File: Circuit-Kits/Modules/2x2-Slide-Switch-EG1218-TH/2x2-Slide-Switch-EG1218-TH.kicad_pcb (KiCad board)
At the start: 2 copper layers, 15.6 x 15.6 mm, 1 part, among them SW1 SPDT_Small

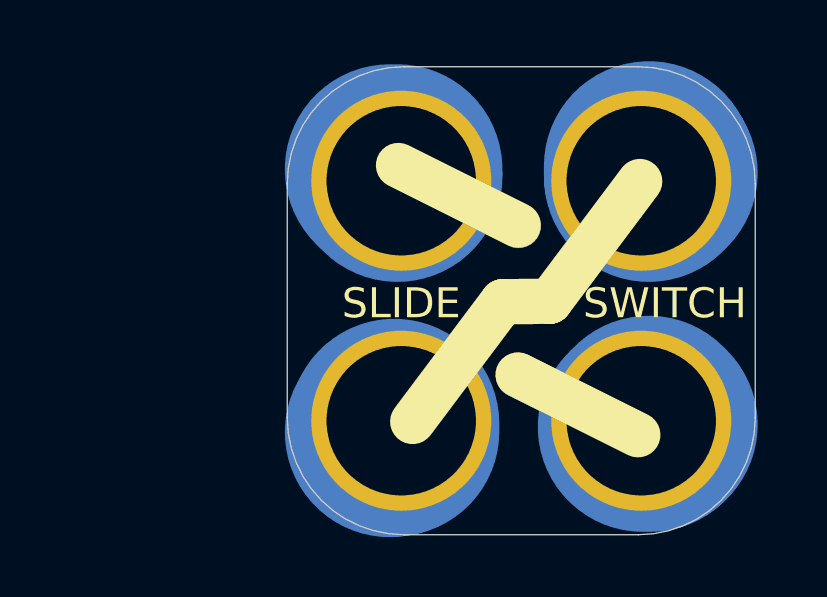
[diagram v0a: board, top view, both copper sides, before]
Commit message: Add top copper rings. Release v1.1 EG1218 TH 2x2
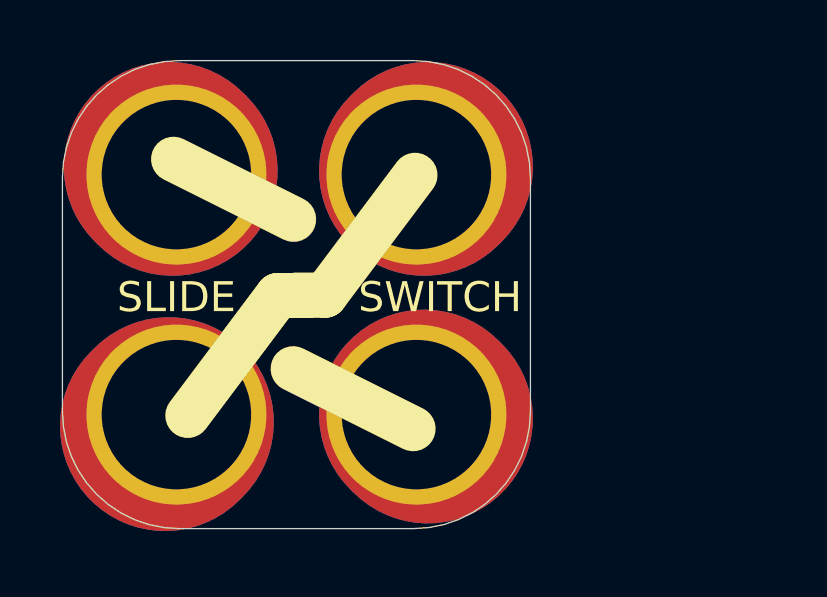
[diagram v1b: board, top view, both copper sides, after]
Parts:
- moved SW1 7.50 mm to (16.5, 57.9)
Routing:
- net /2: track 0.51 -> 0.00 mm
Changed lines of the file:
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@@
     (links 4)
     (no_connects 4)
-    (area 104.572999 74.854999 178.510001 123.265001)
+    (area 2.159 45.877599 145.003759 150.368)
     (thickness 1.6)
-    (drawings 5)
-    (tracks 5)
+    (drawings 1)
+    (tracks 0)
     (zones 0)
     (modules 1)
@@
     (title "2x2 Slide Switch (EG1218)")
     (date "18 Jan 2017")
-    (rev 1.0)
+    (rev "v1.1")
     (company "All rights reserved.")
-    (comment 1 help@browndoggadgets.com)
-    (comment 2 http://browndoggadgets.com/)
+    (comment 1 "help@browndoggadgets.com")
+    (comment 2 "http://browndoggadgets.com/")
     (comment 3 "Brown Dog Gadgets")
   )
@@
   )
   (module Crazy_Circuits:SWITCH-SPDT-3PIN-2.5mmPITCH-TH-2x2 (layer F.Cu)
-    (at 24.004 58.1152)
+    (at 16.51 57.911)
     (descr http://spec_sheets.e-switch.com/specs/P040040.pdf)
     (tags "SWITCH SPDT EG1218 2x3")
@@
       (effects (font (size 1 1) (thickness 0.15)))
     )
-    (fp_line (start 8.255 -8.128) (end 8.382 -8.255) (layer B.Cu) (width 7))
+    (fp_circle (center 7.988591 -8.001) (end 10.274591 -6.985) (layer F.Mask) (width 1.2))
+    (fp_line (start 8.255 -8.128) (end 8.382 -8.255) (layer F.Cu) (width 7))
     (fp_circle (center -0.031267 -8.001) (end 1.238733 -7.4676) (layer F.Fab) (width 0.2))
     (fp_text user 1 (at 8.0264 -0.1016) (layer F.Fab)
@@
     (fp_circle (center 7.969733 0) (end 9.239733 0.5334) (layer F.Fab) (width 0.2))
     (fp_line (start 8.255 -8.128) (end 8.382 -8.255) (layer B.Mask) (width 7))
-    (fp_line (start -0.127 -8.128) (end -0.254 -8.255) (layer B.Cu) (width 7))
+    (fp_line (start -0.127 -8.128) (end -0.254 -8.255) (layer F.Cu) (width 7))
     (fp_line (start -0.127 -8.128) (end -0.254 -8.255) (layer B.Mask) (width 7))
-    (fp_line (start -0.254 0.254) (end -0.381 0.381) (layer B.Cu) (width 7))
+    (fp_line (start -0.254 0.254) (end -0.381 0.381) (layer F.Cu) (width 7))
     (fp_line (start -0.254 0.254) (end -0.381 0.381) (layer B.Mask) (width 7))
     (fp_line (start 8.255 0) (end 8.382 0.127) (layer B.Cu) (width 7))
     (fp_line (start 8.255 0) (end 8.382 0.127) (layer B.Mask) (width 7))
+    (fp_line (start 8.255 -8.128) (end 8.382 -8.255) (layer B.Cu) (width 7))
+    (fp_line (start -0.127 -8.128) (end -0.254 -8.255) (layer B.Cu) (width 7))
+    (fp_line (start -0.254 0.254) (end -0.381 0.381) (layer B.Cu) (width 7))
+    (fp_line (start 8.255 0) (end 8.382 0.127) (layer F.Cu) (width 7))
+    (fp_circle (center 7.988591 0) (end 10.274591 1.016) (layer F.Mask) (width 1.2))
+    (fp_circle (center -0.025109 0) (end 2.260891 1.016) (layer F.Mask) (width 1.2))
+    (fp_circle (center -0.025109 -8.001) (end 2.260891 -6.985) (layer F.Mask) (width 1.2))
     (pad 2 thru_hole circle (at 8 -8) (size 6 6) (drill 4.98) (layers *.Cu B.Mask)
       (net 1 /2))
@@
     (effects (font (size 2.54 2.54) (thickness 0.254)) (justify left))
   )
-  (gr_line (start 32.0929 58.3057) (end 32.1564 58.3692) (layer B.Mask) (width 7))
-  (gr_line (start 23.8379 58.2549) (end 23.7744 58.3184) (layer B.Mask) (width 7))
-  (gr_line (start 23.7871 49.8221) (end 23.7236 49.7586) (layer B.Mask) (width 7))
-  (gr_line (start 32.1691 49.8221) (end 32.2326 49.7586) (layer B.Mask) (width 7))
-  (segment (start 32.258 49.6316) (end 32.258 49.8856) (width 7) (layer B.Cu) (net 1))
-  (segment (start 31.9786 50.0126) (end 31.9786 50.0136) (width 0.254) (layer B.Cu) (net 1))
-  (segment (start 23.7744 58.4708) (end 23.7744 58.2168) (width 7) (layer B.Cu) (net 1))
-  (segment (start 23.622 49.7332) (end 23.876 49.7332) (width 7) (layer B.Cu) (net 2))
-  (segment (start 32.3088 58.3184) (end 32.0548 58.3184) (width 7) (layer B.Cu) (net 3))
 )
